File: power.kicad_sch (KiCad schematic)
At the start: 65 parts, among them J3 LOAD, Q1 AO3401A, Q2 AO3401A, Q21 FS8205A, Q6 2N7002, U10 BQ27546, U27 TPS63001, U29 BQ24081, U30 DW01+G, U6 TPS61040DBV

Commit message: Add second light sensor position for reversed device mounting
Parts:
- J3: now not fitted
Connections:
- net +BATT: now also J3.2 (Pin_2); no longer J3.1 (Pin_1)
- net GND: now also J3.1 (Pin_1); no longer J3.2 (Pin_2)
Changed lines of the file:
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@@
     )
   )
-  (symbol (lib_id "Connector_Generic:Conn_01x02") (at 138.43 33.02 90) (unit 1)
-    (in_bom yes) (on_board yes) (dnp no) (fields_autoplaced)
-    (property "Reference" "J3" (at 143.002 31.996 90)
+  (symbol (lib_id "Connector_Generic:Conn_01x02") (at 140.97 33.02 270) (mirror x) (unit 1)
+    (in_bom yes) (on_board yes) (dnp yes)
+    (property "Reference" "J3" (at 136.398 31.996 90)
       (effects (font (size 1.27 1.27)) (justify right))
     )
-    (property "Value" "LOAD" (at 143.002 34.044 90)
+    (property "Value" "LOAD" (at 136.398 34.044 90)
       (effects (font (size 1.27 1.27)) (justify right))
     )
-    (property "Footprint" "Connector_PinHeader_2.54mm:PinHeader_1x02_P2.54mm_Vertical" (at 138.43 33.02 0)
+    (property "Footprint" "Connector_PinHeader_2.54mm:PinHeader_1x02_P2.54mm_Vertical" (at 140.97 33.02 0)
       (effects (font (size 1.27 1.27)) hide)
     )
-    (property "Datasheet" "~" (at 138.43 33.02 0)
+    (property "Datasheet" "~" (at 140.97 33.02 0)
       (effects (font (size 1.27 1.27)) hide)
     )

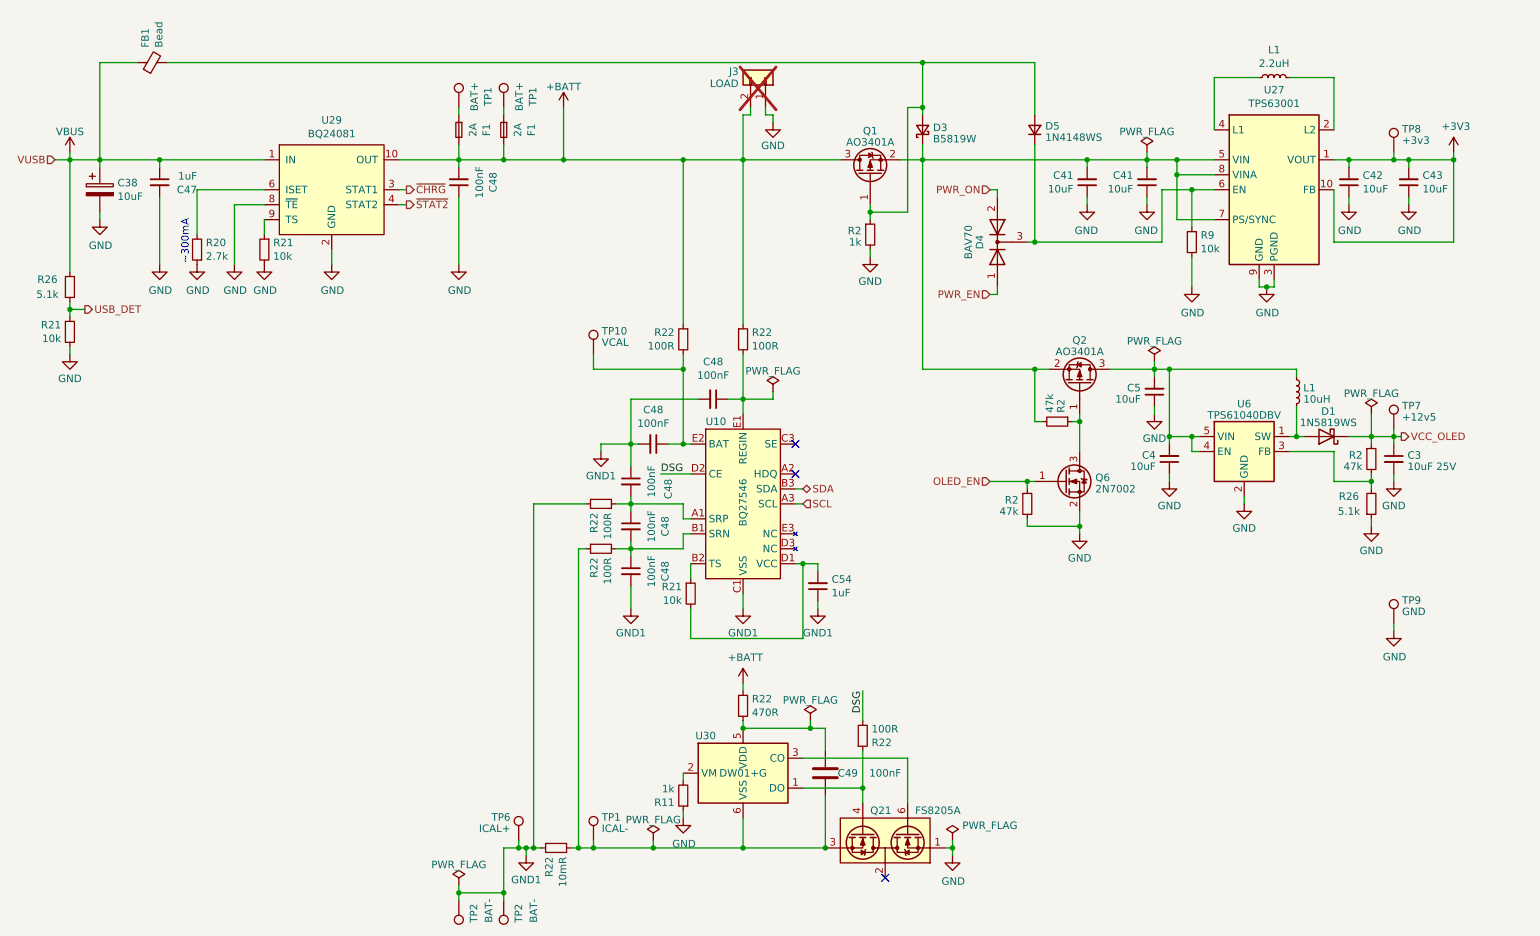
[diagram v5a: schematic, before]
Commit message: Do rough component placement
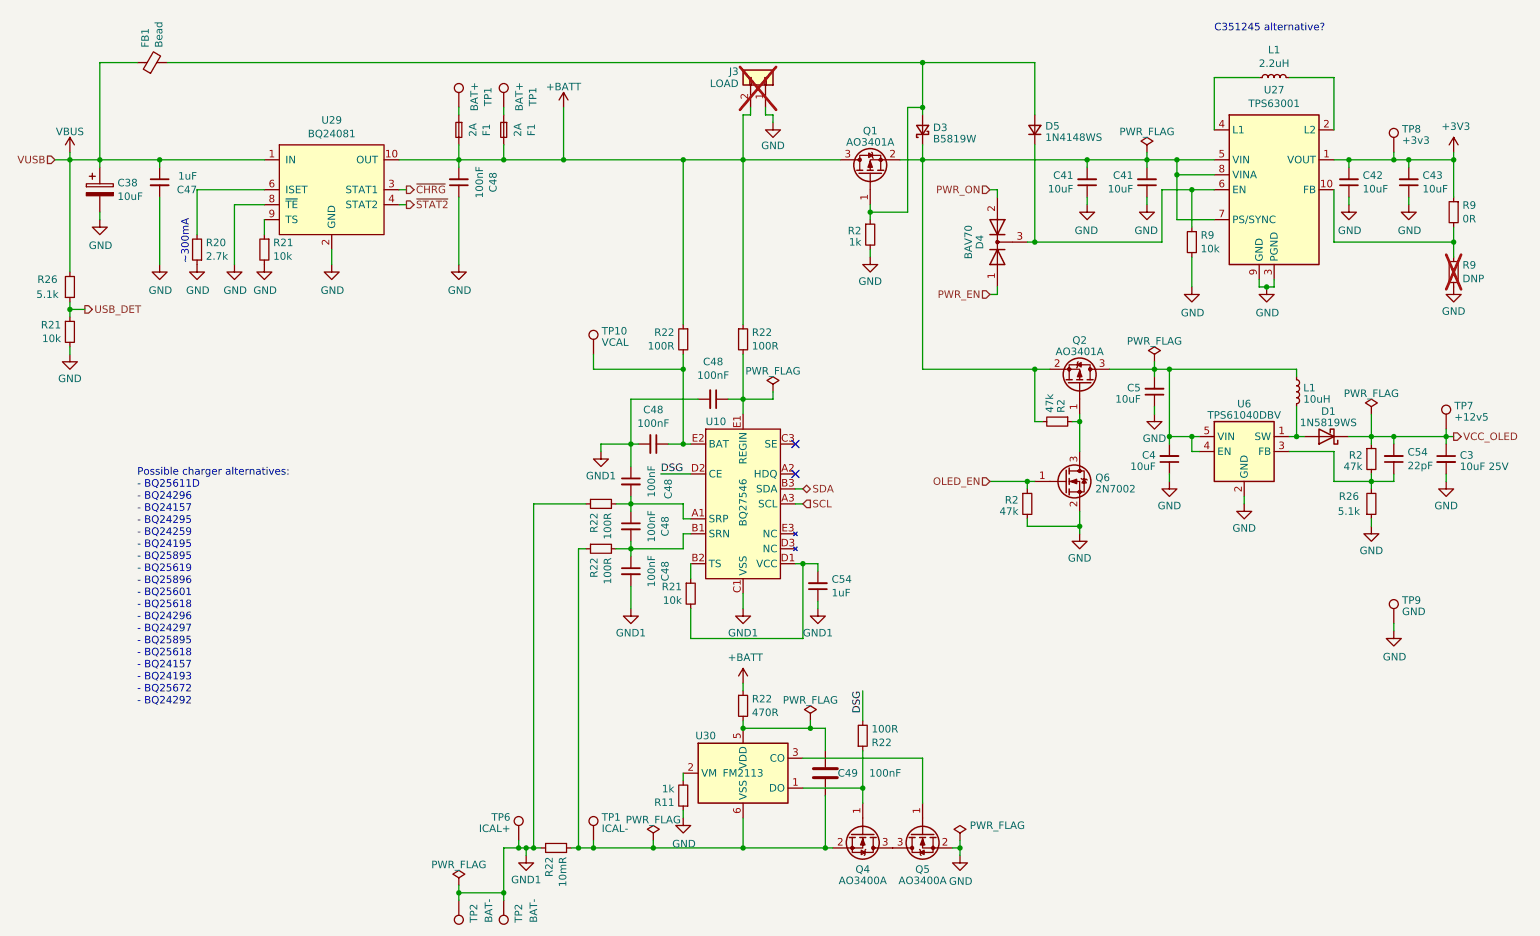
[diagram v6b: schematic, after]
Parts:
- removed Q21: FS8205A, Package_TO_SOT_SMD:SOT-23-6, symbol Transistor_FET_Dual:FS8205
- added C54: 22pF, Capacitor_SMD:C_0402_1005Metric, symbol Device:C_Small
- added Q4, Q5: AO3400A, Package_TO_SOT_SMD:SOT-23, symbol Transistor_FET:AO3400A
- added R9: DNP, Resistor_SMD:R_0402_1005Metric, symbol Device:R_Small
- added R9: 0R, Resistor_SMD:R_0402_1005Metric, symbol Device:R_Small
- L1: footprint Inductor_SMD:L_1210_3225Metric -> Inductor_SMD:L_Taiyo-Yuden_MD-3030; LCSC C703786 -> C329596
- U30: value DW01+G -> FM2113; LCSC C14213 -> C2832124
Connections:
- net +3V3: now also R9.1; no longer U27.10 (FB)
- net GND: now also Q5.2 (S), R9.2
- net VCC_OLED: now also C54.2
- net at C49.1, R22.1, R22.2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: now also Q4.2 (S)
- net at R22.1, U30.1 (DO): now also Q4.1 (G)
- net at U30.3 (CO): now also Q5.1 (G)
- net at R2.2, R26.2, U6.3 (FB): now also C54.1
- new net: R9.1, R9.2, U27.10 (FB)
- new net: Q4.3 (D), Q5.3 (D)
- no-connect marks 3 -> 2
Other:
- note added: "C351245 alternative?"
- note added: "Possible charger alternatives: - BQ25611D - BQ24296 - BQ24157 - BQ24295 - BQ24259 - BQ24195 - BQ25895 - BQ25619 - BQ25896 - BQ25601 - BQ25618 - BQ24296 - BQ24297 - BQ25895 - BQ25618 - BQ24157 - BQ24193 - BQ25672 - BQ24292"
- moved on the sheet: C3, TP7

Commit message: Finsh first layout iteration
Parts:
- removed TP9: GND, TestPoint:TestPoint_Pad_1.0x1.0mm, symbol Connector:TestPoint
- added C48: 100nF, Capacitor_SMD:C_0402_1005Metric, symbol Device:C_Small
- added C54: DNP, Capacitor_SMD:C_0402_1005Metric, symbol Device:C_Small
- added R21 (x3): DNP, Resistor_SMD:R_0402_1005Metric, symbol Device:R_Small
- TP1: footprint TestPoint:TestPoint_Pad_1.0x1.0mm -> TestPoint:TestPoint_Pad_1.5x1.5mm
- TP10, TP6: footprint TestPoint:TestPoint_Pad_1.0x1.0mm -> TestPoint:TestPoint_Pad_2.0x2.0mm
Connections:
- net GND: now also C48.1, C54.1, R21.2
- net PWR_EN: now also D4.2 (A); no longer D4.1 (A)
- net PWR_ON: now also D4.3 (K), D5.1 (K), R9.1, U27.6 (EN); no longer D4.2 (A)
- net VBUS: now also FB1.2; no longer FB1.1
- net at D3.2 (A), D5.2 (A), Q1.1 (G)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: now also FB1.1; no longer FB1.2
- net at C41.2, C41.2, D3.1 (K)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: now also C48.2
- net at R20.2, U29.6 (ISET): now also R21.2
- new net: C54.2, R21.1, R21.1, R21.1
- new net ISET: R21.2
- new net PWR_ON2: D4.1 (A)
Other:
- moved on the sheet: C3, C38, C4, C41, C42, C43, C47, C48, C49, C5, C54, D1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
